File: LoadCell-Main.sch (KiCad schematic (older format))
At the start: 19 parts, among them J1 Vin, J2 GND, J3 WHT, J4 GRN, J5 RED, J6 BLK, J7 Vout, J8 GND, U1 L78L12ABUTR, U2 LM321SN3T1G

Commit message: Single circuit placed
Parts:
- removed J1: Vin, _Connector:0.100_1x1_small, symbol 1x1
- removed J2, J8: GND, _Connector:0.100_1x1_small, symbol 1x1
- removed J7: Vout, _Connector:0.100_1x1_small, symbol 1x1
- D1: value D_ZENER -> MM3Z3V0ST1G
- J1: renamed from P?; value CONN_02X02 -> M20-8760242; footprint (none) -> _Connector:Pin_Header_Straight_2x02_Pitch2.54mm_SMD
- renumbered J3 to J2, J4 to J3, J5 to J4, J6 to J5
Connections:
- net labels added: Vin, Vout
- wire segments 27 -> 32
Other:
- moved on the sheet: J1
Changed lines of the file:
@@
 U 1 1 5A80CDDA
 P 2400 1600
-F 0 "U1" H 2100 1850 50  0000 C CNN
+F 0 "U1" H 2400 1900 50  0000 C CNN
 F 1 "L78L12ABUTR" H 2400 1800 50  0000 C CNN
 F 2 "_Active:SOT89-3" H 2400 1700 50  0000 C CIN
@@
 $EndComp
 $Comp
-L 1x1 J1
-U 1 1 5A80E60C
-P 1450 1550
-F 0 "J1" H 1450 1650 50  0000 C CNN
-F 1 "Vin" V 1550 1550 50  0000 C CNN
-F 2 "_Connector:0.100_1x1_small" H 1450 1550 50  0001 C CNN
-F 3 "" H 1450 1550 50  0000 C CNN
-	1    1450 1550
-	-1   0    0    1
-$EndComp
-$Comp
 L 1x1 J2
-U 1 1 5A80E653
-P 1450 1950
-F 0 "J2" H 1450 2050 50  0000 C CNN
-F 1 "GND" V 1550 1950 50  0000 C CNN
-F 2 "_Connector:0.100_1x1_small" H 1450 1950 50  0001 C CNN
-F 3 "" H 1450 1950 50  0000 C CNN
-	1    1450 1950
-	-1   0    0    1
-$EndComp
-$Comp
-L 1x1 J5
-U 1 1 5A80E6A7
-P 3300 1550
-F 0 "J5" H 3300 1650 50  0000 C CNN
-F 1 "RED" V 3400 1550 50  0000 C CNN
-F 2 "_Connector:0.100_1x1_small" H 3300 1550 50  0001 C CNN
-F 3 "" H 3300 1550 50  0000 C CNN
-	1    3300 1550
-	1    0    0    -1
-$EndComp
-$Comp
-L 1x1 J6
-U 1 1 5A80E6D0
-P 3300 1950
-F 0 "J6" H 3300 2050 50  0000 C CNN
-F 1 "BLK" V 3400 1950 50  0000 C CNN
-F 2 "_Connector:0.100_1x1_small" H 3300 1950 50  0001 C CNN
-F 3 "" H 3300 1950 50  0000 C CNN
-	1    3300 1950
-	1    0    0    -1
-$EndComp
-$Comp
-L 1x1 J3
 U 1 1 5A80E6FC
 P 1450 3250
-F 0 "J3" H 1450 3150 50  0000 C CNN
+F 0 "J2" H 1450 3150 50  0000 C CNN
 F 1 "WHT" V 1550 3250 50  0000 C CNN
 F 2 "_Connector:0.100_1x1_small" H 1450 3250 50  0001 C CNN
@@
 $EndComp
 $Comp
-L 1x1 J4
+L 1x1 J3
 U 1 1 5A80E72B
 P 1450 3450
-F 0 "J4" H 1450 3550 50  0000 C CNN
+F 0 "J3" H 1450 3550 50  0000 C CNN
 F 1 "GRN" V 1550 3450 50  0000 C CNN
 F 2 "_Connector:0.100_1x1_small" H 1450 3450 50  0001 C CNN
@@
 	1    1450 3450
 	-1   0    0    1
-$EndComp
-$Comp
-L 1x1 J8
-U 1 1 5A80E761
-P 3550 3550
-F 0 "J8" H 3550 3450 50  0000 C CNN
-F 1 "GND" V 3650 3550 50  0000 C CNN
-F 2 "_Connector:0.100_1x1_small" H 3550 3550 50  0001 C CNN
-F 3 "" H 3550 3550 50  0000 C CNN
-	1    3550 3550
-	1    0    0    -1
 $EndComp
 $Comp
@@
 $EndComp
 $Comp
-L 1x1 J7
-U 1 1 5A80E9E3
-P 3550 3350
-F 0 "J7" H 3550 3450 50  0000 C CNN
-F 1 "Vout" V 3650 3350 50  0000 C CNN
-F 2 "_Connector:0.100_1x1_small" H 3550 3350 50  0001 C CNN
-F 3 "" H 3550 3350 50  0000 C CNN
-	1    3550 3350
-	1    0    0    -1
-$EndComp
-$Comp
 L R R5
 U 1 1 5A80EB34
@@
 U 1 1 5A80F3F0
 P 2400 3350
-F 0 "U2" H 2370 3580 50  0000 L CNN
+F 0 "U2" H 2400 3500 50  0000 L CNN
 F 1 "LM321SN3T1G" H 2330 3140 50  0000 L CNN
 F 2 "_Active:SOT-23-5" H 2400 3350 50  0001 C CNN
@@
 $EndComp
 Wire Wire Line
-	1650 1550 1950 1550
-Wire Wire Line
 	1800 1600 1800 1550
 Connection ~ 1800 1550
@@
 Connection ~ 3000 1550
 Wire Wire Line
-	1650 1950 3100 1950
-Wire Wire Line
-	3000 1900 3000 1950
+	3000 1950 3000 1900
 Connection ~ 3000 1950
 Wire Wire Line
 	2400 1900 2400 2000
 Connection ~ 2400 1950
-Wire Wire Line
-	1800 1900 1800 1950
 Connection ~ 1800 1950
 Wire Wire Line
@@
 Wire Wire Line
 	2050 3850 2050 3900
-Wire Wire Line
-	2050 3900 3300 3900
 Connection ~ 2300 3900
 Wire Wire Line
@@
 	2750 2950 2750 3350
 Connection ~ 2750 3350
-Wire Wire Line
-	3100 3350 3350 3350
-Wire Wire Line
-	3300 3900 3300 3550
-Wire Wire Line
-	3300 3550 3350 3550
-Wire Wire Line
-	3150 3550 3150 3350
 Connection ~ 3150 3350
 Wire Wire Line
-	3150 3750 3150 3900
+	3150 3900 3150 3750
 Connection ~ 3150 3900
 $Comp
@@
 P 3150 3650
 F 0 "D1" H 3150 3750 50  0000 C CNN
-F 1 "D_ZENER" H 3150 3550 50  0000 C CNN
+F 1 "MM3Z3V0ST1G" V 3500 3650 50  0000 C CNN
 F 2 "_Passive:SOD-323" H 3150 3650 50  0001 C CNN
 F 3 "" H 3150 3650 50  0000 C CNN
@@
 $EndComp
 $Comp
-L CONN_02X02 P?
+L CONN_02X02 J1
 U 1 1 5A81E132
-P 2400 2450
-F 0 "P?" H 2400 2600 50  0000 C CNN
-F 1 "CONN_02X02" H 2400 2300 50  0000 C CNN
-F 2 "" H 2400 1250 50  0000 C CNN
-F 3 "" H 2400 1250 50  0000 C CNN
-	1    2400 2450
-	1    0    0    -1
-$EndComp
+P 1450 2450
+F 0 "J1" H 1450 2600 50  0000 C CNN
+F 1 "M20-8760242" H 1450 2300 50  0000 C CNN
+F 2 "_Connector:Pin_Header_Straight_2x02_Pitch2.54mm_SMD" H 1450 1250 50  0001 C CNN
+F 3 "" H 1450 1250 50  0000 C CNN
+	1    1450 2450
+	1    0    0    -1
+$EndComp
+$Comp
+L 1x1 J5
+U 1 1 5A80E6D0
+P 3300 1950
+F 0 "J5" H 3300 2050 50  0000 C CNN
+F 1 "BLK" V 3400 1950 50  0000 C CNN
+F 2 "_Connector:0.100_1x1_small" H 3300 1950 50  0001 C CNN
+F 3 "" H 3300 1950 50  0000 C CNN
+	1    3300 1950
+	1    0    0    -1
+$EndComp
+$Comp
+L 1x1 J4
+U 1 1 5A80E6A7
+P 3300 1550
+F 0 "J4" H 3300 1650 50  0000 C CNN
+F 1 "RED" V 3400 1550 50  0000 C CNN
+F 2 "_Connector:0.100_1x1_small" H 3300 1550 50  0001 C CNN
+F 3 "" H 3300 1550 50  0000 C CNN
+	1    3300 1550
+	1    0    0    -1
+$EndComp
+Wire Wire Line
+	1150 1950 3100 1950
+Wire Wire Line
+	1050 1550 1950 1550
+Wire Wire Line
+	2050 3900 3350 3900
+Wire Wire Line
+	3350 3900 3350 2400
+Wire Wire Line
+	3100 3350 3150 3350
+Text Label 1250 1550 0    60   ~ 0
+Vin
+Text Label 1250 1950 0    60   ~ 0
+GND
+Wire Wire Line
+	3350 2400 1700 2400
+Wire Wire Line
+	1700 2500 3150 2500
+Wire Wire Line
+	3150 2500 3150 3550
+Text Label 1800 2400 0    60   ~ 0
+GND
+Text Label 1800 2500 0    60   ~ 0
+Vout
+Wire Wire Line
+	1200 2400 1150 2400
+Wire Wire Line
+	1150 2400 1150 1950
+Wire Wire Line
+	1800 1900 1800 1950
+Wire Wire Line
+	1050 1550 1050 2500
+Wire Wire Line
+	1050 2500 1200 2500
 $EndSCHEMATC

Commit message: Revised circuit. Schematic revised, layout not yet.
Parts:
- removed J2: WHT, _Connector:0.100_1x1_small, symbol 1x1
- removed J3: GRN, _Connector:0.100_1x1_small, symbol 1x1
- removed J4: RED, _Connector:0.100_1x1_small, symbol 1x1
- removed J5: BLK, _Connector:0.100_1x1_small, symbol 1x1
- removed R2: 100R, _Passive:R_0402, symbol R
- added C3, C4, C5, C6, C7, C8: 1uF, _Passive:C_0402, symbol C
- added D2, D3, D4: MM3Z3V0ST1G, _Passive:SOD-323, symbol D_ZENER
- added J2, J4, J6, J8: 0.100_1X4, symbol 0.100_1X4
- added J3, J5, J7: M20-8760242, _Connector:Pin_Header_Straight_2x02_Pitch2.54mm_SMD, symbol CONN_02X02
- added R10, R14, R6: 1K, _Passive:R_0402, symbol R
- added R11, R12, R15, R16, R7, R8: 100R, _Passive:R_0402, symbol R
- added R13, R5, R9: 270K, _Passive:R_0402, symbol R
- added U3, U5, U7: L78L12ABUTR, _Active:SOT89-3, symbol L78L12ABUTR
- added U4, U6, U8: LM321SN3T1G, _Active:SOT-23-5, symbol LM321_23-5
- R1: renamed from R4; value 10K -> 270K
- R2: renamed from R1; value 100R -> 1K
- R4: renamed from R3; value 10K -> 100R
- renumbered R5 to R3
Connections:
- net labels added: BLK, GRN, RED, VL+, VL-, Vopo, WHT
- net labels removed: +12V
- wire segments 32 -> 136
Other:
- moved on the sheet: C1, C2, D1, J1, R1, R2, R3, R4, U1, U2

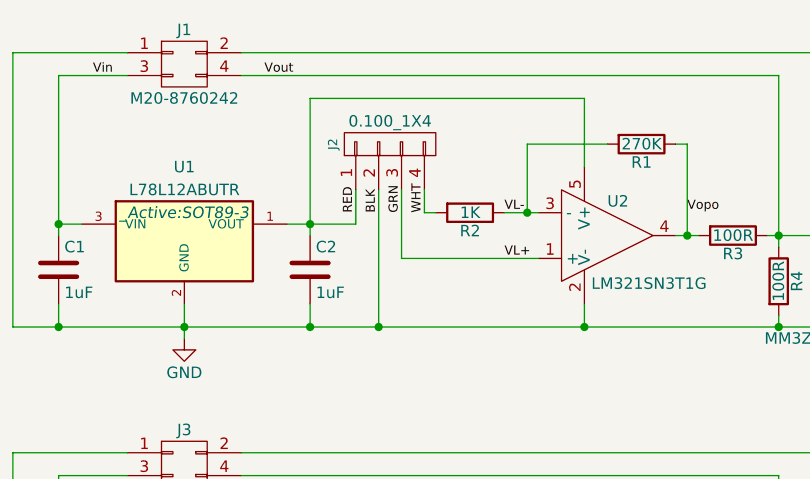
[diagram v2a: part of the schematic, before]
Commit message: Changed load cell termination pads
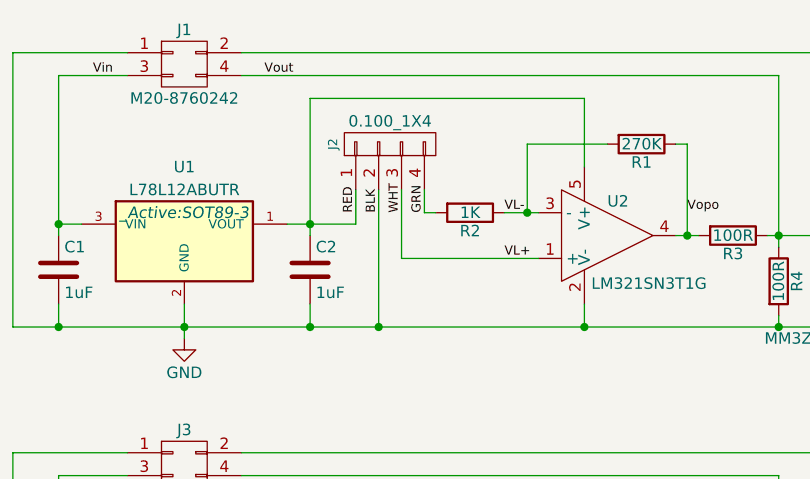
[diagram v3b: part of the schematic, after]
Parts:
- J2, J4, J6, J8: footprint (none) -> _Connector:0.100_1x4_micro
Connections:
- net WHT is gone; now on net GRN: J2.4 (P4), R2.2
- net GRN: no longer J2.3 (P3), U2.1 (+)
- new net VL+: J2.3 (P3), U2.1 (+)
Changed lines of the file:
@@
 F 0 "J2" H 4200 1450 40  0000 C CNN
 F 1 "0.100_1X4" V 4300 1200 50  0000 C CNN
-F 2 "" H 4200 1200 50  0000 C CNN
+F 2 "_Connector:0.100_1x4_micro" H 4200 1200 50  0001 C CNN
 F 3 "" H 4200 1200 50  0000 C CNN
 	1    4200 1200
@@
 Text Label 4150 1500 1    40   ~ 0
 BLK
+Text Label 4350 1500 1    40   ~ 0
+GRN
 Text Label 4250 1500 1    40   ~ 0
-GRN
-Text Label 4350 1500 1    40   ~ 0
 WHT
 $Comp
@@
 F 0 "J4" H 4200 3200 40  0000 C CNN
 F 1 "0.100_1X4" V 4300 2950 50  0000 C CNN
-F 2 "" H 4200 2950 50  0000 C CNN
+F 2 "_Connector:0.100_1x4_micro" H 4200 2950 50  0001 C CNN
 F 3 "" H 4200 2950 50  0000 C CNN
 	1    4200 2950
@@
 F 0 "J6" H 4200 5050 40  0000 C CNN
 F 1 "0.100_1X4" V 4300 4800 50  0000 C CNN
-F 2 "" H 4200 4800 50  0000 C CNN
+F 2 "_Connector:0.100_1x4_micro" H 4200 4800 50  0001 C CNN
 F 3 "" H 4200 4800 50  0000 C CNN
 	1    4200 4800
@@
 F 0 "J8" H 4200 6900 40  0000 C CNN
 F 1 "0.100_1X4" V 4300 6650 50  0000 C CNN
-F 2 "" H 4200 6650 50  0000 C CNN
+F 2 "_Connector:0.100_1x4_micro" H 4200 6650 50  0001 C CNN
 F 3 "" H 4200 6650 50  0000 C CNN
 	1    4200 6650

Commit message: Added fiducials, final check
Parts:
- added FID1, FID2, FID3: Fiducial_Top, _Connector:Fiducial_0.040_Top, symbol Fiducial_Top
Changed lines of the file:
@@
 Sheet 2 2
 Title "LoadCell Amplifier Circuit"
-Date "15-Feb-2018"
+Date "20-Feb-2018"
 Rev "revA"
 Comp "Ten Mile Square"
@@
 $EndComp
 $Comp
-L GND #PWR1
+L GND #PWR01
 U 1 1 5A80EBC4
 P 3300 2050
-F 0 "#PWR1" H 3300 1800 50  0001 C CNN
+F 0 "#PWR01" H 3300 1800 50  0001 C CNN
 F 1 "GND" H 3300 1900 50  0000 C CNN
 F 2 "" H 3300 2050 50  0000 C CNN
@@
 $EndComp
 $Comp
-L GND #PWR2
+L GND #PWR02
 U 1 1 5A866D04
 P 3300 3800
-F 0 "#PWR2" H 3300 3550 50  0001 C CNN
+F 0 "#PWR02" H 3300 3550 50  0001 C CNN
 F 1 "GND" H 3300 3650 50  0000 C CNN
 F 2 "" H 3300 3800 50  0000 C CNN
@@
 $EndComp
 $Comp
-L GND #PWR3
+L GND #PWR03
 U 1 1 5A8670E2
 P 3300 5650
-F 0 "#PWR3" H 3300 5400 50  0001 C CNN
+F 0 "#PWR03" H 3300 5400 50  0001 C CNN
 F 1 "GND" H 3300 5500 50  0000 C CNN
 F 2 "" H 3300 5650 50  0000 C CNN
@@
 $EndComp
 $Comp
-L GND #PWR4
+L GND #PWR04
 U 1 1 5A8675A9
 P 3300 7500
-F 0 "#PWR4" H 3300 7250 50  0001 C CNN
+F 0 "#PWR04" H 3300 7250 50  0001 C CNN
 F 1 "GND" H 3300 7350 50  0000 C CNN
 F 2 "" H 3300 7500 50  0000 C CNN
@@
 	6300 6250 6300 7450
 Connection ~ 6100 7450
+$Comp
+L Fiducial_Top FID1
+U 1 1 5A8C10DE
+P 7850 1200
+F 0 "FID1" H 7850 1300 40  0000 C CNN
+F 1 "Fiducial_Top" H 7850 1100 40  0000 C CNN
+F 2 "_Connector:Fiducial_0.040_Top" H 7850 1200 150 0001 C CNN
+F 3 "" H 7850 1200 150 0000 C CNN
+	1    7850 1200
+	1    0    0    -1
+$EndComp
+$Comp
+L Fiducial_Top FID2
+U 1 1 5A8C1162
+P 7850 1600
+F 0 "FID2" H 7850 1700 40  0000 C CNN
+F 1 "Fiducial_Top" H 7850 1500 40  0000 C CNN
+F 2 "_Connector:Fiducial_0.040_Top" H 7850 1600 150 0001 C CNN
+F 3 "" H 7850 1600 150 0000 C CNN
+	1    7850 1600
+	1    0    0    -1
+$EndComp
+$Comp
+L Fiducial_Top FID3
+U 1 1 5A8C11D3
+P 7850 2000
+F 0 "FID3" H 7850 2100 40  0000 C CNN
+F 1 "Fiducial_Top" H 7850 1900 40  0000 C CNN
+F 2 "_Connector:Fiducial_0.040_Top" H 7850 2000 150 0001 C CNN
+F 3 "" H 7850 2000 150 0000 C CNN
+	1    7850 2000
+	1    0    0    -1
+$EndComp
 $EndSCHEMATC

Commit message: Started changes the version 2
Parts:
- removed U1: L78L12ABUTR, _Active:SOT89-3, symbol L78L12ABUTR
- removed U2: LM321SN3T1G, _Active:SOT-23-5, symbol LM321_23-5
- added U? (x2): MCP6002, symbol MCP6002
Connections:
- wire segments 136 -> 127
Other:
- moved on the sheet: C2, D1, FID1, FID2, FID3, J2, R1, R2, R3, R4
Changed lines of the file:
@@
 L C C2
 U 1 1 5A80CCD0
-P 3850 1750
-F 0 "C2" H 3875 1850 50  0000 L CNN
-F 1 "1uF" H 3875 1650 50  0000 L CNN
-F 2 "_Passive:C_0402" H 3888 1600 50  0001 C CNN
-F 3 "" H 3850 1750 50  0000 C CNN
-	1    3850 1750
+P 7550 1200
+F 0 "C2" H 7575 1300 50  0000 L CNN
+F 1 "1uF" H 7575 1100 50  0000 L CNN
+F 2 "_Passive:C_0402" H 7588 1050 50  0001 C CNN
+F 3 "" H 7550 1200 50  0000 C CNN
+	1    7550 1200
 	1    0    0    -1
 $EndComp
@@
 L R R4
 U 1 1 5A80CD03
-P 5900 1800
-F 0 "R4" V 5980 1800 50  0000 C CNN
-F 1 "100R" V 5900 1800 50  0000 C CNN
-F 2 "_Passive:R_0402" V 5830 1800 50  0001 C CNN
-F 3 "" H 5900 1800 50  0000 C CNN
-	1    5900 1800
-	1    0    0    -1
-$EndComp
-$Comp
-L L78L12ABUTR U1
-U 1 1 5A80CDDA
-P 3300 1600
-F 0 "U1" H 3300 1900 50  0000 C CNN
-F 1 "L78L12ABUTR" H 3300 1800 50  0000 C CNN
-F 2 "_Active:SOT89-3" H 3300 1700 50  0000 C CIN
-F 3 "" H 3300 1600 50  0000 C CNN
-	1    3300 1600
+P 8100 1100
+F 0 "R4" V 8180 1100 50  0000 C CNN
+F 1 "100R" V 8100 1100 50  0000 C CNN
+F 2 "_Passive:R_0402" V 8030 1100 50  0001 C CNN
+F 3 "" H 8100 1100 50  0000 C CNN
+	1    8100 1100
 	1    0    0    -1
 $EndComp
@@
 L R R3
 U 1 1 5A80EB34
-P 5700 1600
-F 0 "R3" V 5780 1600 50  0000 C CNN
-F 1 "100R" V 5700 1600 50  0000 C CNN
-F 2 "_Passive:R_0402" V 5630 1600 50  0001 C CNN
-F 3 "" H 5700 1600 50  0000 C CNN
-	1    5700 1600
-	0    1    1    0
+P 7850 800
+F 0 "R3" V 7930 800 50  0000 C CNN
+F 1 "100R" V 7850 800 50  0000 C CNN
+F 2 "_Passive:R_0402" V 7780 800 50  0001 C CNN
+F 3 "" H 7850 800 50  0000 C CNN
+	1    7850 800
+	1    0    0    -1
 $EndComp
 $Comp
@@
 L R R1
 U 1 1 5A80EC35
-P 5300 1200
-F 0 "R1" V 5380 1200 50  0000 C CNN
-F 1 "270K" V 5300 1200 50  0000 C CNN
-F 2 "_Passive:R_0402" V 5230 1200 50  0001 C CNN
-F 3 "" H 5300 1200 50  0000 C CNN
-	1    5300 1200
-	0    1    1    0
+P 4450 1400
+F 0 "R1" V 4530 1400 50  0000 C CNN
+F 1 "270K" V 4450 1400 50  0000 C CNN
+F 2 "_Passive:R_0402" V 4380 1400 50  0001 C CNN
+F 3 "" H 4450 1400 50  0000 C CNN
+	1    4450 1400
+	-1   0    0    1
 $EndComp
 $Comp
 L R R2
 U 1 1 5A80EC7B
-P 4550 1500
-F 0 "R2" V 4630 1500 50  0000 C CNN
-F 1 "1K" V 4550 1500 50  0000 C CNN
-F 2 "_Passive:R_0402" V 4480 1500 50  0001 C CNN
-F 3 "" H 4550 1500 50  0000 C CNN
-	1    4550 1500
-	0    1    1    0
-$EndComp
-$Comp
-L LM321_23-5 U2
-U 1 1 5A80F3F0
-P 5150 1600
-F 0 "U2" H 5150 1750 50  0000 L CNN
-F 1 "LM321SN3T1G" H 5080 1390 50  0000 L CNN
-F 2 "_Active:SOT-23-5" H 5150 1600 50  0001 C CNN
-F 3 "" H 5150 1600 50  0000 C CNN
-	1    5150 1600
-	1    0    0    -1
+P 4450 1800
+F 0 "R2" V 4530 1800 50  0000 C CNN
+F 1 "1K" V 4450 1800 50  0000 C CNN
+F 2 "_Passive:R_0402" V 4380 1800 50  0001 C CNN
+F 3 "" H 4450 1800 50  0000 C CNN
+	1    4450 1800
+	-1   0    0    1
 $EndComp
 $Comp
 L D_ZENER D1
 U 1 1 5A81D761
-P 6100 1800
-F 0 "D1" H 6100 1900 50  0000 C CNN
-F 1 "MM3Z3V0ST1G" V 6350 1800 50  0000 C CNN
-F 2 "_Passive:SOD-323" H 6100 1800 50  0001 C CNN
-F 3 "" H 6100 1800 50  0000 C CNN
-	1    6100 1800
+P 7800 1800
+F 0 "D1" H 7800 1900 50  0000 C CNN
+F 1 "MM3Z3V0ST1G" V 8050 1800 50  0000 C CNN
+F 2 "_Passive:SOD-323" H 7800 1800 50  0001 C CNN
+F 3 "" H 7800 1800 50  0000 C CNN
+	1    7800 1800
 	0    1    1    0
 $EndComp
@@
 Text Label 3650 900  0    40   ~ 0
 Vout
-Text Label 4700 1500 0    40   ~ 0
+Text Label 2200 1100 0    40   ~ 0
 VL-
-Text Label 4700 1700 0    40   ~ 0
+Text Label 2200 1200 0    40   ~ 0
 VL+
-Text Label 5500 1500 0    40   ~ 0
+Text Label 2150 1300 0    40   ~ 0
 Vopo
 $Comp
 L 0.100_1X4 J2
 U 1 1 5A85E78B
-P 4200 1200
-F 0 "J2" H 4200 1450 40  0000 C CNN
-F 1 "0.100_1X4" V 4300 1200 50  0000 C CNN
-F 2 "_Connector:0.100_1x4_micro" H 4200 1200 50  0001 C CNN
-F 3 "" H 4200 1200 50  0000 C CNN
-	1    4200 1200
-	0    -1   -1   0
-$EndComp
-Text Label 4050 1500 1    40   ~ 0
+P 3300 1750
+F 0 "J2" H 3300 2000 40  0000 C CNN
+F 1 "0.100_1X4" V 3400 1750 50  0000 C CNN
+F 2 "_Connector:0.100_1x4_micro" H 3300 1750 50  0001 C CNN
+F 3 "" H 3300 1750 50  0000 C CNN
+	1    3300 1750
+	0    -1   1    0
+$EndComp
+Text Label 3150 1200 3    40   ~ 0
 RED
-Text Label 4150 1500 1    40   ~ 0
+Text Label 3250 1200 3    40   ~ 0
 BLK
-Text Label 4350 1500 1    40   ~ 0
+Text Label 3450 1200 3    40   ~ 0
 GRN
-Text Label 4250 1500 1    40   ~ 0
+Text Label 5200 1400 0    40   ~ 0
 WHT
 $Comp
@@
 Wire Wire Line
 	2750 900  2750 1600
-Connection ~ 2750 1550
-Wire Wire Line
-	4700 1500 4850 1500
-Wire Wire Line
-	5150 1200 4800 1200
-Wire Wire Line
-	4800 1200 4800 1500
-Connection ~ 4800 1500
-Wire Wire Line
-	5450 1600 5550 1600
-Wire Wire Line
-	5450 1200 5500 1200
-Wire Wire Line
-	5500 1200 5500 1600
-Connection ~ 5500 1600
-Connection ~ 5900 1600
 Connection ~ 5900 2000
 Wire Wire Line
-	5850 1600 6100 1600
-Wire Wire Line
 	2750 1900 2750 2000
 Wire Wire Line
 	5900 2000 5900 1950
 Wire Wire Line
-	6100 1600 6100 1700
-Wire Wire Line
 	6100 2000 6100 1900
 Wire Wire Line
 	3050 900  2750 900
 Wire Wire Line
-	2850 1550 2750 1550
-Wire Wire Line
 	2550 800  3050 800
-Wire Wire Line
-	3750 1550 4050 1550
-Connection ~ 3850 1550
-Wire Wire Line
-	3850 2000 3850 1900
-Wire Wire Line
-	4050 1550 4050 1400
-Wire Wire Line
-	3850 1000 3850 1600
-Wire Wire Line
-	4150 2000 4150 1400
-Wire Wire Line
-	3850 1000 5050 1000
-Wire Wire Line
-	5050 1000 5050 1300
-Wire Wire Line
-	4350 1400 4350 1500
-Wire Wire Line
-	4350 1500 4400 1500
-Wire Wire Line
-	4850 1700 4250 1700
-Wire Wire Line
-	4250 1700 4250 1400
 Wire Wire Line
 	2550 2000 6300 2000
 Connection ~ 2750 2000
 Wire Wire Line
-	3300 1900 3300 2050
-Connection ~ 3300 2000
-Connection ~ 3850 2000
-Connection ~ 4150 2000
-Wire Wire Line
-	5050 1900 5050 2000
-Connection ~ 5050 2000
-Wire Wire Line
 	3550 900  5900 900
-Wire Wire Line
-	5900 900  5900 1650
 Wire Wire Line
 	3550 800  6300 800
@@
 Wire Wire Line
 	5900 6350 5900 7100
-Wire Wire Line
-	6300 800  6300 2000
 Connection ~ 6100 2000
 Wire Wire Line
@@
 L Fiducial_Top FID1
 U 1 1 5A8C10DE
-P 7850 1200
-F 0 "FID1" H 7850 1300 40  0000 C CNN
-F 1 "Fiducial_Top" H 7850 1100 40  0000 C CNN
-F 2 "_Connector:Fiducial_0.040_Top" H 7850 1200 150 0001 C CNN
-F 3 "" H 7850 1200 150 0000 C CNN
-	1    7850 1200
+P 1050 800
+F 0 "FID1" H 1050 900 40  0000 C CNN
+F 1 "Fiducial_Top" H 1050 700 40  0000 C CNN
+F 2 "_Connector:Fiducial_0.040_Top" H 1050 800 150 0001 C CNN
+F 3 "" H 1050 800 150 0000 C CNN
+	1    1050 800
 	1    0    0    -1
 $EndComp
@@
 L Fiducial_Top FID2
 U 1 1 5A8C1162
-P 7850 1600
-F 0 "FID2" H 7850 1700 40  0000 C CNN
-F 1 "Fiducial_Top" H 7850 1500 40  0000 C CNN
-F 2 "_Connector:Fiducial_0.040_Top" H 7850 1600 150 0001 C CNN
-F 3 "" H 7850 1600 150 0000 C CNN
-	1    7850 1600
+P 1050 1200
+F 0 "FID2" H 1050 1300 40  0000 C CNN
+F 1 "Fiducial_Top" H 1050 1100 40  0000 C CNN
+F 2 "_Connector:Fiducial_0.040_Top" H 1050 1200 150 0001 C CNN
+F 3 "" H 1050 1200 150 0000 C CNN
+	1    1050 1200
 	1    0    0    -1
 $EndComp
@@
 L Fiducial_Top FID3
 U 1 1 5A8C11D3
-P 7850 2000
-F 0 "FID3" H 7850 2100 40  0000 C CNN
-F 1 "Fiducial_Top" H 7850 1900 40  0000 C CNN
-F 2 "_Connector:Fiducial_0.040_Top" H 7850 2000 150 0001 C CNN
-F 3 "" H 7850 2000 150 0000 C CNN
-	1    7850 2000
-	1    0    0    -1
-$EndComp
+P 1050 1600
+F 0 "FID3" H 1050 1700 40  0000 C CNN
+F 1 "Fiducial_Top" H 1050 1500 40  0000 C CNN
+F 2 "_Connector:Fiducial_0.040_Top" H 1050 1600 150 0001 C CNN
+F 3 "" H 1050 1600 150 0000 C CNN
+	1    1050 1600
+	1    0    0    -1
+$EndComp
+$Comp
+L MCP6002 U?
+U 1 1 5ADCF38B
+P 4100 1250
+F 0 "U?" H 4100 1400 50  0000 L CNN
+F 1 "MCP6002" H 4100 1500 50  0000 L CNN
+F 2 "" H 4000 1300 50  0000 C CNN
+F 3 "" H 4100 1400 50  0000 C CNN
+	1    4100 1250
+	1    0    0    -1
+$EndComp
+$Comp
+L MCP6002 U?
+U 2 1 5ADCF54D
+P 8800 1300
+F 0 "U?" H 8800 1450 50  0000 L CNN
+F 1 "MCP6002" H 8800 1150 50  0000 L CNN
+F 2 "" H 8700 1350 50  0000 C CNN
+F 3 "" H 8800 1450 50  0000 C CNN
+	2    8800 1300
+	1    0    0    -1
+$EndComp
+Wire Wire Line
+	3150 1200 3150 1550
+Wire Wire Line
+	2750 1200 3150 1200
+Connection ~ 2750 1200
+Wire Wire Line
+	3250 1150 3250 1550
+Wire Wire Line
+	2900 1150 3250 1150
+Wire Wire Line
+	2900 1150 2900 2000
+Connection ~ 2900 2000
+Wire Wire Line
+	4000 950  4000 900
+Connection ~ 4000 900
+Wire Wire Line
+	4000 1550 4000 2000
+Connection ~ 4000 2000
+Wire Wire Line
+	4400 1250 4450 1250
+Wire Wire Line
+	4450 1550 4450 1650
+Wire Wire Line
+	4450 1950 4450 2000
+Connection ~ 4450 2000
+Wire Wire Line
+	3800 1350 3750 1350
+Wire Wire Line
+	3750 1350 3750 1600
+Wire Wire Line
+	3750 1600 4450 1600
+Connection ~ 4450 1600
+Wire Wire Line
+	3450 1550 3450 1150
+Wire Wire Line
+	3450 1150 3800 1150
 $EndSCHEMATC

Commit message: Checkpoint
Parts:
- removed R3, R4: 100R, _Passive:R_0402, symbol R
- added R?: 1K, _Passive:R_0603, symbol R
- added R?: 270K, _Passive:R_0603, symbol R
- C1, C2: footprint _Passive:C_0402 -> _Passive:C_0603
- R1: value 270K -> 390K; footprint _Passive:R_0402 -> _Passive:R_0603
- R2: footprint _Passive:R_0402 -> _Passive:R_0603
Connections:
- net labels added: Vcc
- net labels removed: Vin
- wire segments 127 -> 207
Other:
- moved on the sheet: C1, C2, D1, J1, J2, U?B
